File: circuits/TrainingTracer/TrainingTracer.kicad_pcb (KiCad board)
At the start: 2 copper layers, 131 x 100 mm, 64 parts, among them J1 BATT+, J10 Conn_01x01_Socket, J11 BMX055/BNO055-1, J12 BMX055/BNO055-2, J13 OLED_DSP, J14 DRV8835_1, J15 DRV8835_2, J16 PINHD-1x6(MOTOR-L), J17 PINHD-1x6(MOTO-R), J18 NUCLEO-F303K8, J19 NUCLEO-F303K8, J2 BATT-, J20 SDL, J21 SCL, J3 Conn_01x01_Socket, J4 Conn_01x01_Socket, J5 Conn_01x01_Socket, J6 Conn_01x01_Socket, J7 Conn_01x01_Socket, J8 Conn_01x01_Socket, J9 Conn_01x01_Socket, SW1 SW_SPDT, SW2 SW1, SW3 SW2, U1 NJU7223F-33, U2 LM2931-3.3_TO220

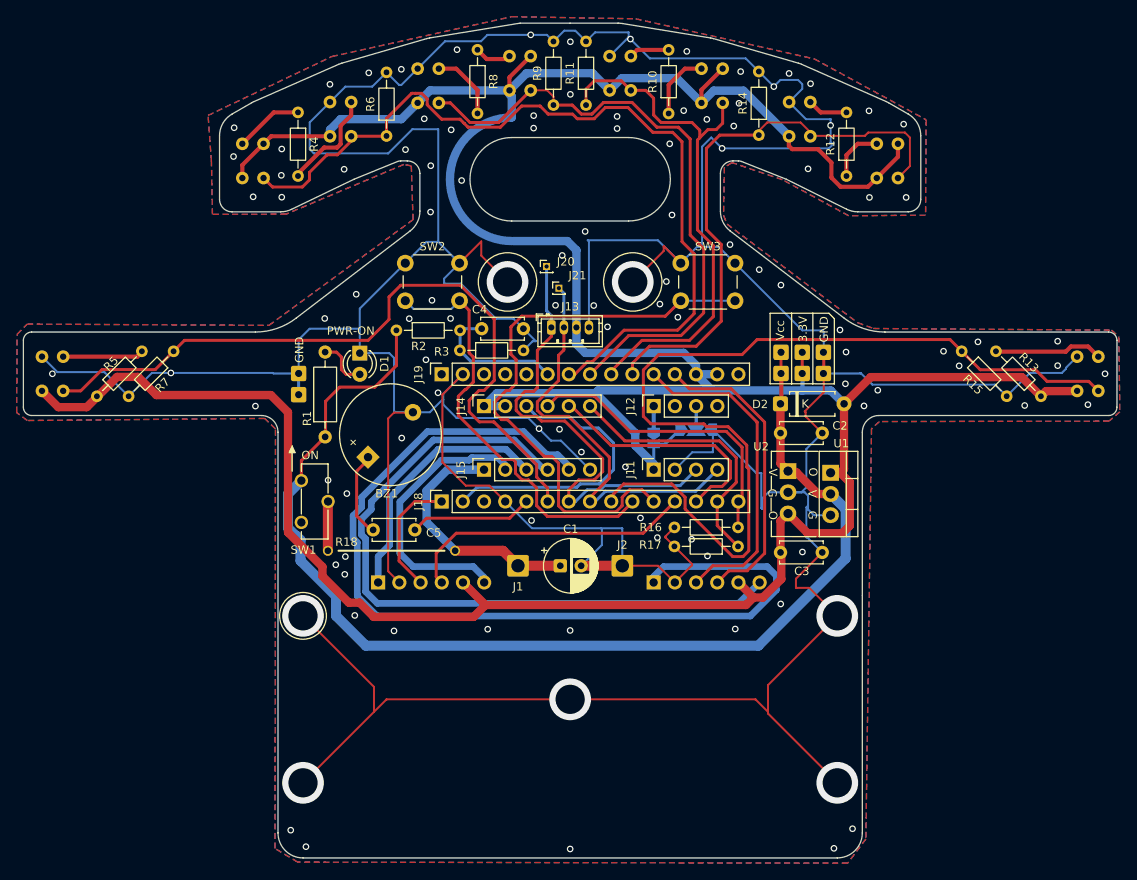
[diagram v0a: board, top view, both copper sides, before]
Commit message: PCBのPDF出力
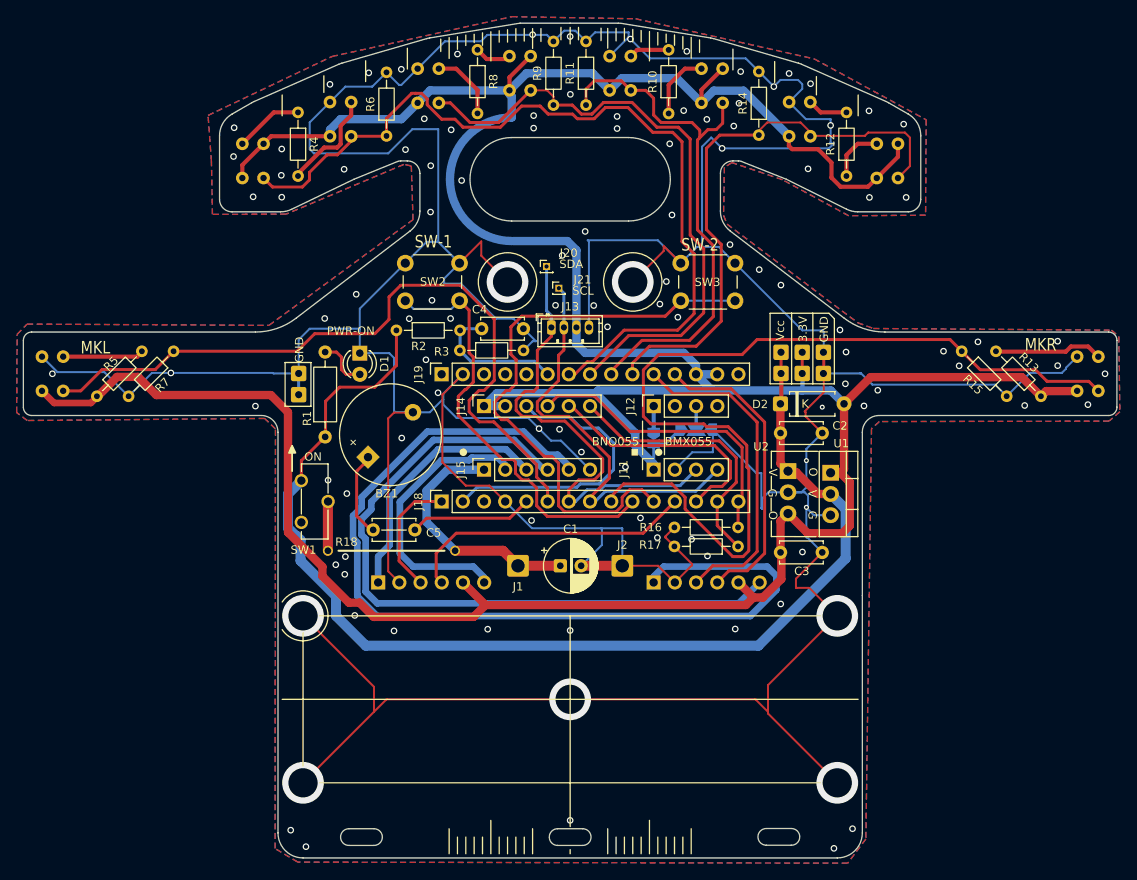
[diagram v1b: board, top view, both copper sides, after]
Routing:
- net GND: vias 111 -> 114
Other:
- outline, holes or cut-outs redrawn
- board text added: "BMX055"
- board text added: "BMX● BNO■"
- board text added: "BNO055"
- board text added: "Black"
- board text added: "Blue"
- board text added: "Green"
- board text added: "MKL"
- board text added: "MKR"
- board text added: "Red"
- board text added: "SCL"
- board text added: "SDA"
- board text added: "SW-1"
- board text added: "SW-2"
- board text added: "White"
- board text added: "Yellow"

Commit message: ゴミファイル削除。PDFの移動。
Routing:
- net SW2: track 69.1 -> 70.6 mm
- net GND: vias 114 -> 115

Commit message: PCB後進
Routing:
- net GND: track 644.5 -> 650.3 mm, vias 115 -> 120
- net MLS: track 88.5 -> 89.6 mm
- net +3.3V: track 407.1 -> 406.1 mm
- net AIN2: track 36.2 -> 37.0 mm
- net LLS: track 102.6 -> 103.2 mm
- net Net-(PR8-K): track 6.70 -> 6.05 mm
- net FLS: track 75.0 -> 75.5 mm
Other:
- outline, holes or cut-outs redrawn
- board text added: "TrainingTracerV2+α"
